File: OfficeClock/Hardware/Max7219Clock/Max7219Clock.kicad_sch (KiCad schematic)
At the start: 4 parts, among them U1 ESP32-C6-Super-Mini

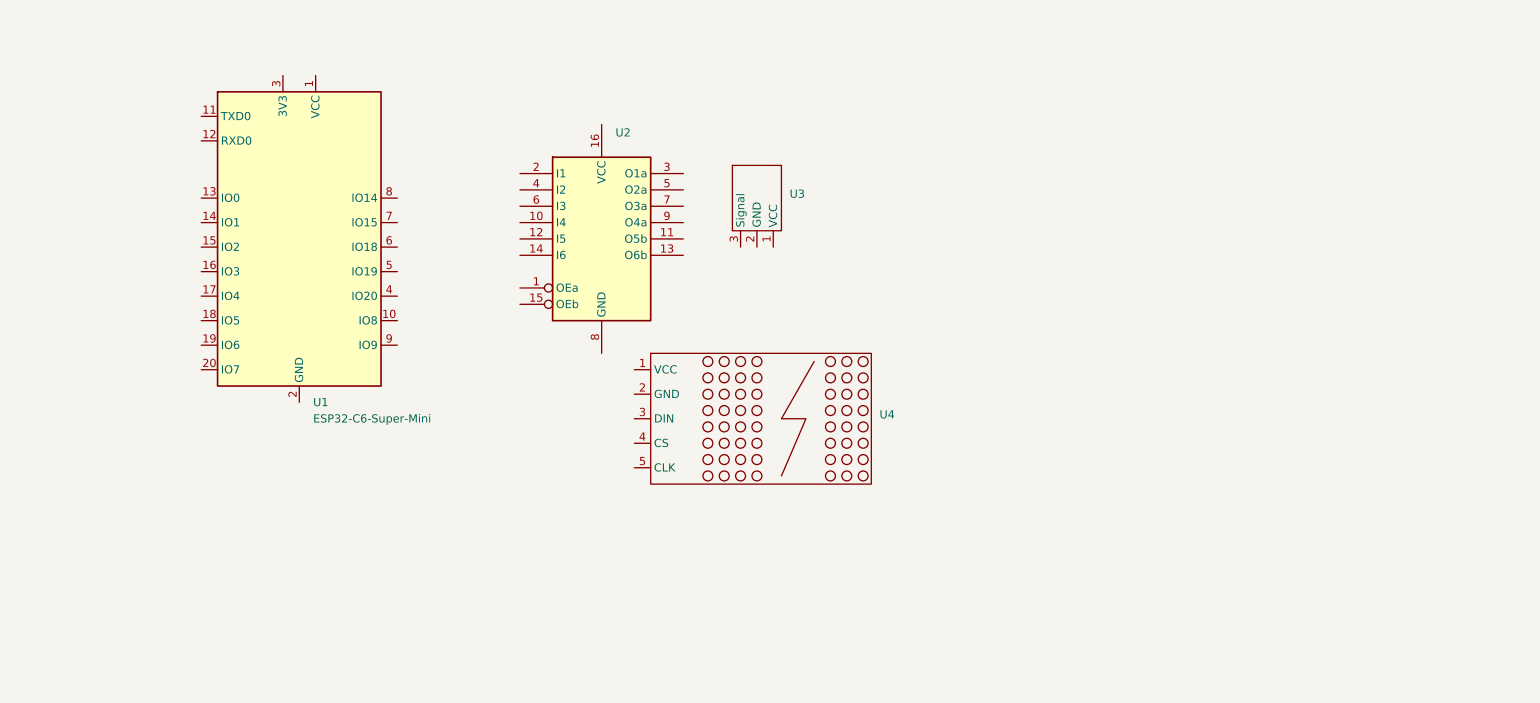
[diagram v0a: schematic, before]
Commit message: Updates to hardware design
Mostly finished. Need to check routing
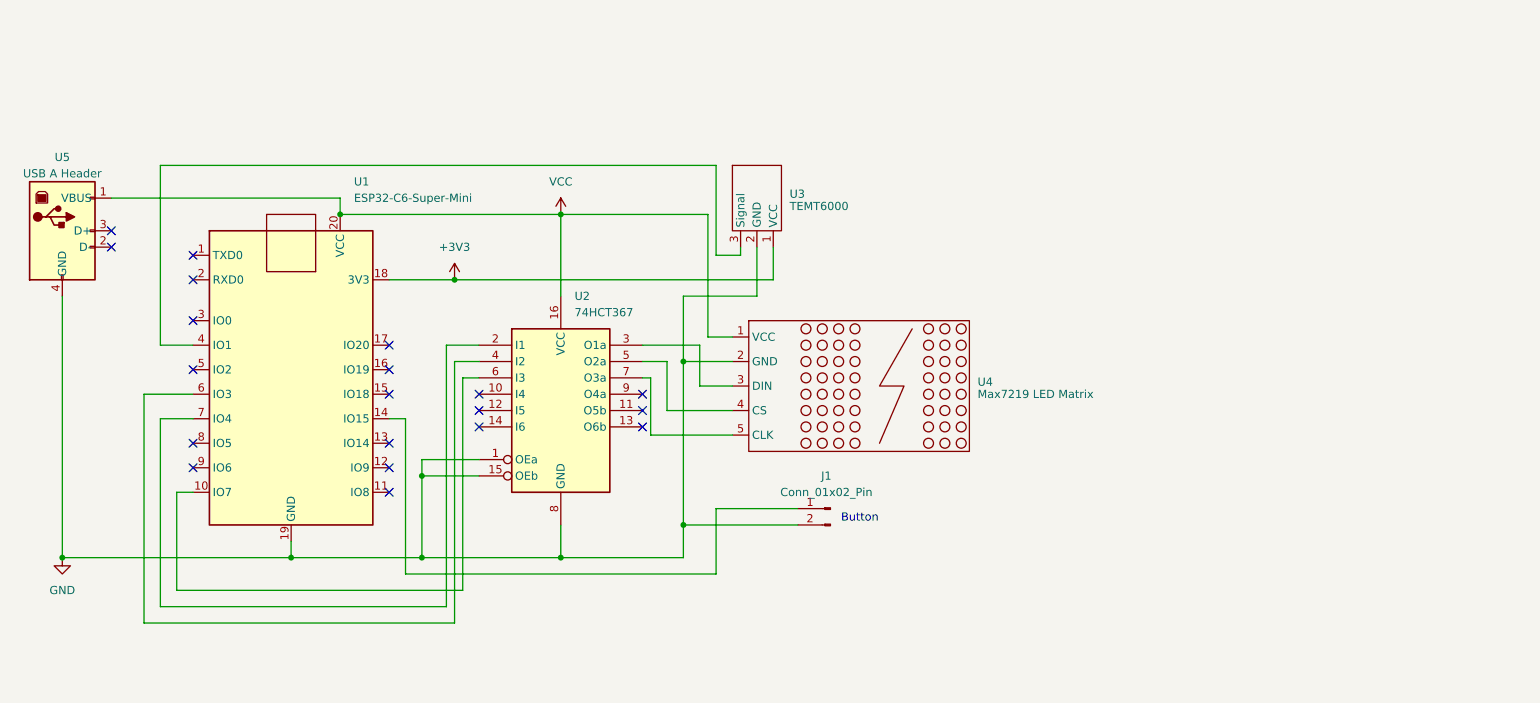
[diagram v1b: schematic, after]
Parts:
- added J1: Conn_01x02_Pin, Connector_PinHeader_2.54mm:PinHeader_1x02_P2.54mm_Vertical, symbol Connector:Conn_01x02_Pin
- added U5: USB A Header, Connector_PinHeader_2.54mm:PinHeader_1x04_P2.54mm_Vertical, symbol Connector:USB_Header
- U1: footprint RF_Module:ESP32-C6-MINI-1 -> Package_DIP:ESP32-C6-SuperMini
- U2: value ~ -> 74HCT367; footprint (none) -> Package_DIP:DIP-16_W7.62mm_Socket
- U3: value ~ -> TEMT6000; footprint (none) -> Connector_PinHeader_2.54mm:PinHeader_1x03_P2.54mm_Vertical
- U4: value ~ -> Max7219 LED Matrix; footprint (none) -> Connector_PinSocket_2.54mm:PinSocket_1x05_P2.54mm_Horizontal
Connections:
- net VCC: now reaches U4.1 (VCC)
- net VCC: now also U1.20 (VCC), U2.16 (VCC), U5.1 (VBUS)
- net GND: now reaches U4.2 (GND)
- net GND: now also U1.19 (GND), U2.1 (OEa), U2.15 (OEb), U2.8 (GND), U3.2 (GND), J1.2 (Pin_2), U5.4 (GND)
- net at U4.3 (DIN): now also U2.3 (O1a)
- net at U4.4 (CS): now also U2.5 (O2a)
- net at U4.5 (CLK): now also U2.7 (O3a)
- net at U2.2 (I1): now also U1.7 (IO4)
- net at U2.4 (I2): now also U1.6 (IO3)
- net at U2.6 (I3): now also U1.10 (IO7)
- net at U1.14 (IO15): now also J1.1 (Pin_1)
- net +3V3: now reaches U1.18 (3V3)
- net +3V3: now also U3.1 (VCC)
- net at U1.4 (IO1): now also U3.3 (Signal)
- no-connect marks 0 -> 20
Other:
- note added: "Button"
- moved on the sheet: U4

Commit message: Updated files and generated final Gerber files for submission
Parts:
- added C1, C2, C3: 0.1uf, Capacitor_THT:C_Disc_D8.0mm_W5.0mm_P5.00mm, symbol Device:C_Small_US
- added H1, H2, H3, H4: MountingHole, MountingHole:MountingHole_2.2mm_M2, symbol Mechanical:MountingHole
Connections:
- net GND: now also J1.1 (Pin_1), C1.2, C2.2, C3.2; no longer J1.2 (Pin_2)
- net VCC: now also C1.1, C2.1, C3.1
- net at U1.10 (IO7): now also U2.4 (I2); no longer U2.6 (I3)
- net at U1.14 (IO15): now also J1.2 (Pin_2); no longer J1.1 (Pin_1)
- net at U1.6 (IO3): now also U2.6 (I3); no longer U2.4 (I2)
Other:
- company: (none) -> MarrinTech
- title: (none) -> LED Matrix Clock
- moved on the sheet: J1, U1, U2, U3, U4, U5
